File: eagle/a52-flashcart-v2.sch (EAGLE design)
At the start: 11 parts

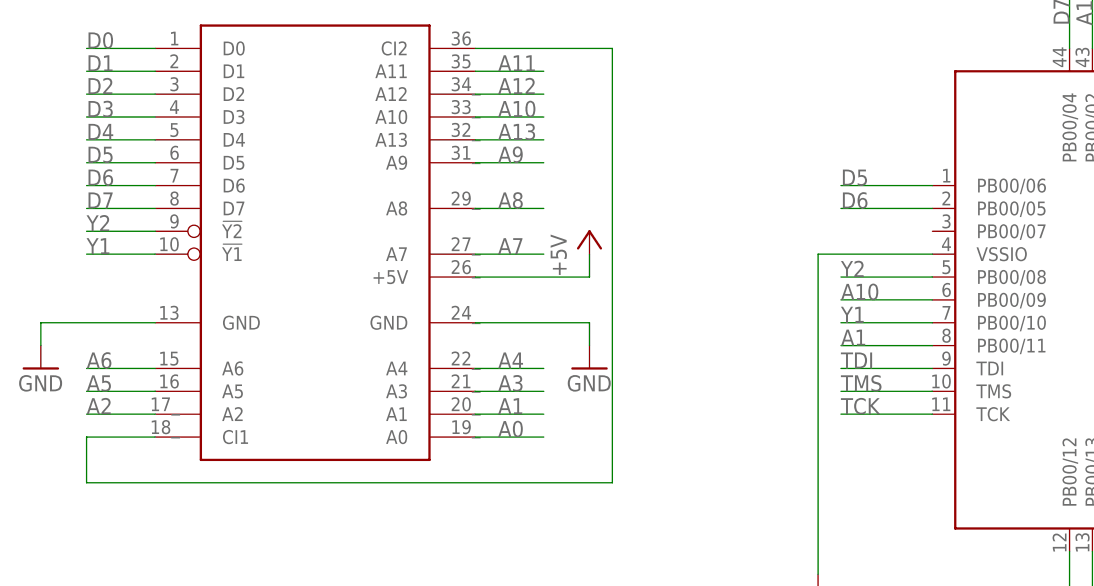
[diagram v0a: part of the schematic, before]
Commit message: board update - PHI2 signal connected to CPLD
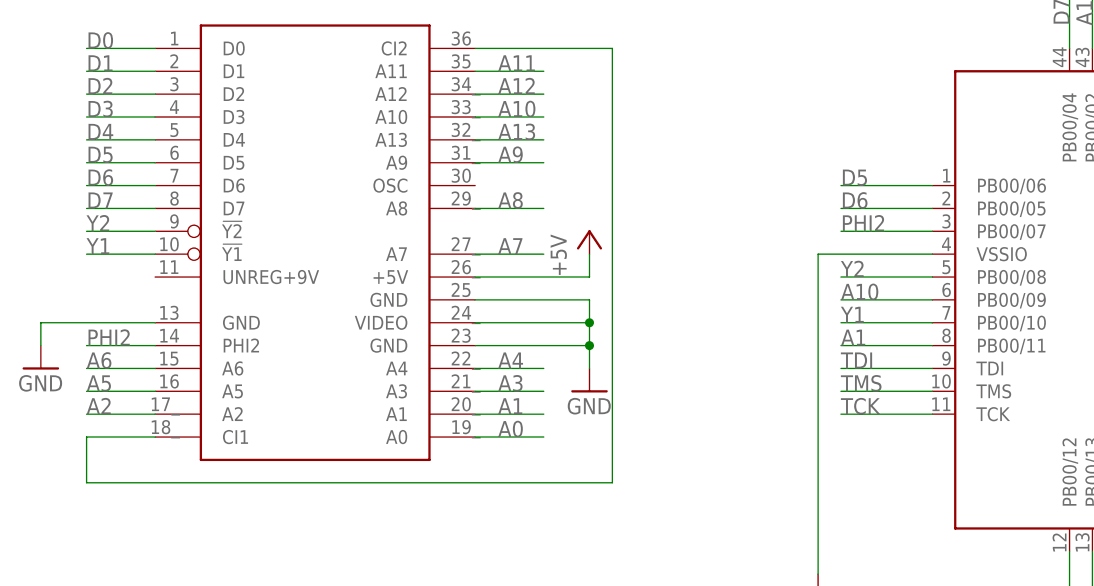
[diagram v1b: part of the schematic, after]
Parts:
- U$1: value ATARI-5200S -> ATARI-5200-TS; device a52-cartridge:ATARI-5200S -> a52-cartridge:ATARI-5200-TS
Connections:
- new net PHI2: U$1.PHI2, XC9536XL.PB00/07
- net GND: now also U$1.GND@23, U$1.GND@25, U$1.VIDEO; no longer U$1.GND@24
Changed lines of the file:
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@@
 <parts>
 <part name="FRAME1" library="frames" deviceset="DINA4_L" device=""/>
-<part name="U$1" library="a52-cartridge" deviceset="ATARI-5200" device="S" value="ATARI-5200S"/>
+<part name="U$1" library="a52-cartridge" deviceset="ATARI-5200-T" device="S" value="ATARI-5200-TS"/>
 <part name="FLASH" library="am29-memory" deviceset="AM29F040J" device=""/>
 <part name="XC9536XL" library="xilinx-xc9" deviceset="XC9536_44VQ" device="" value="XC9536XL"/>
@@
 <instance part="XC9536XL" gate="G$1" x="137.16" y="114.3"/>
 <instance part="GND1" gate="1" x="10.16" y="106.68"/>
-<instance part="GND2" gate="1" x="71.12" y="106.68"/>
+<instance part="GND2" gate="1" x="71.12" y="104.14"/>
 <instance part="P+1" gate="1" x="71.12" y="121.92"/>
 <instance part="+3V1" gate="G$1" x="76.2" y="43.18"/>
@@
 </segment>
 <segment>
-<pinref part="U$1" gate="G$1" pin="GND@24"/>
+<pinref part="U$1" gate="G$1" pin="VIDEO"/>
 <wire x1="58.42" y1="111.76" x2="71.12" y2="111.76" width="0.1524" layer="91"/>
 <wire x1="71.12" y1="111.76" x2="71.12" y2="109.22" width="0.1524" layer="91"/>
 <pinref part="GND2" gate="1" pin="GND"/>
+<pinref part="U$1" gate="G$1" pin="GND@23"/>
+<wire x1="71.12" y1="109.22" x2="71.12" y2="106.68" width="0.1524" layer="91"/>
+<wire x1="58.42" y1="109.22" x2="71.12" y2="109.22" width="0.1524" layer="91"/>
+<junction x="71.12" y="109.22"/>
+<pinref part="U$1" gate="G$1" pin="GND@25"/>
+<wire x1="58.42" y1="114.3" x2="71.12" y2="114.3" width="0.1524" layer="91"/>
+<wire x1="71.12" y1="114.3" x2="71.12" y2="111.76" width="0.1524" layer="91"/>
+<junction x="71.12" y="111.76"/>
 </segment>
 <segment>
@@
 </segment>
 </net>
+<net name="PHI2" class="0">
+<segment>
+<pinref part="U$1" gate="G$1" pin="PHI2"/>
+<wire x1="15.24" y1="109.22" x2="22.86" y2="109.22" width="0.1524" layer="91"/>
+<label x="15.24" y="109.22" size="1.778" layer="95"/>
+</segment>
+<segment>
+<pinref part="XC9536XL" gate="G$1" pin="PB00/07"/>
+<wire x1="99.06" y1="121.92" x2="109.22" y2="121.92" width="0.1524" layer="91"/>
+<label x="99.06" y="121.92" size="1.778" layer="95"/>
+</segment>
+</net>
